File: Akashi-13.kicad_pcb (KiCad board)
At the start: 2 copper layers, 67.3 x 91.4 mm, 5 parts, among them J1 Conn_02x35_Odd_Even, J2 Conn_02x35_Odd_Even, J3 N7E50-Q516RB-50, J4 J0011D01BNL, U1 LAN9220-ABZJ

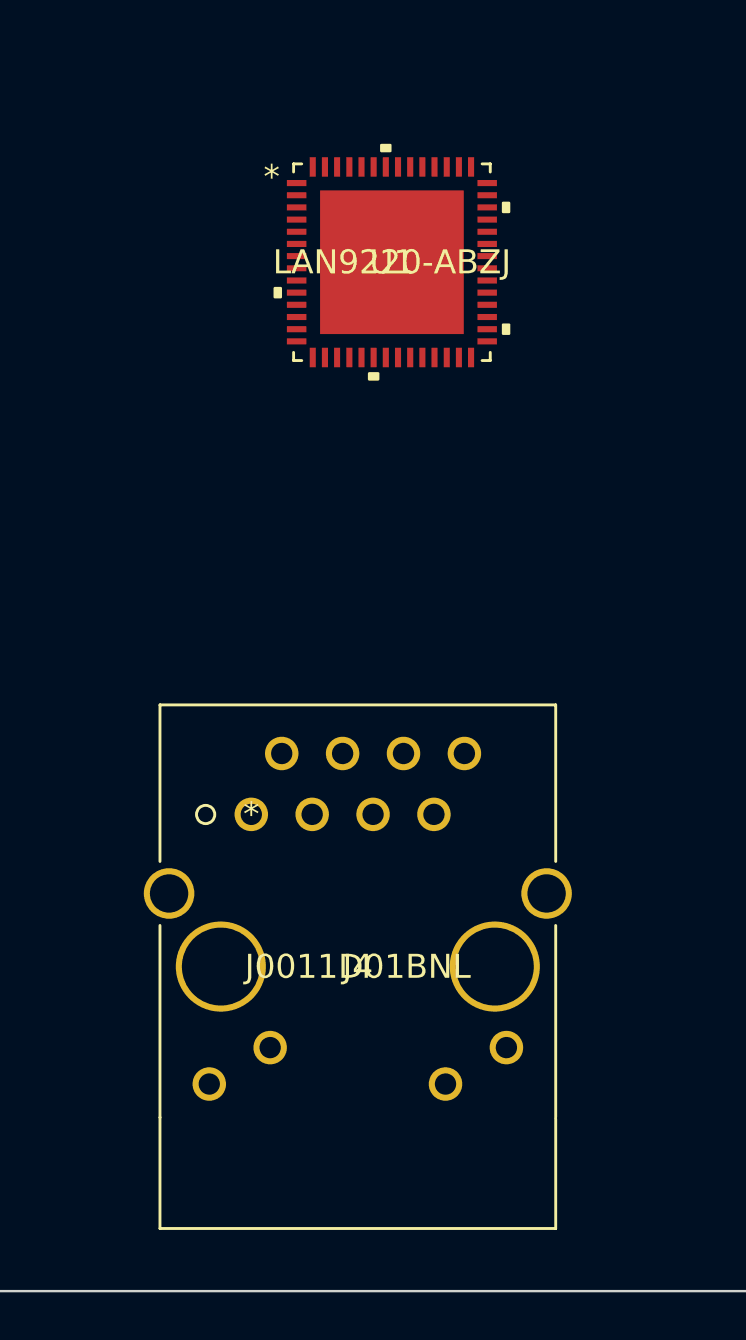
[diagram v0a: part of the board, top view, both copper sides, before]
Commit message: Drawing schematics.
Done round the RF-45 connectors.

Connecting the power of the LAN9220.
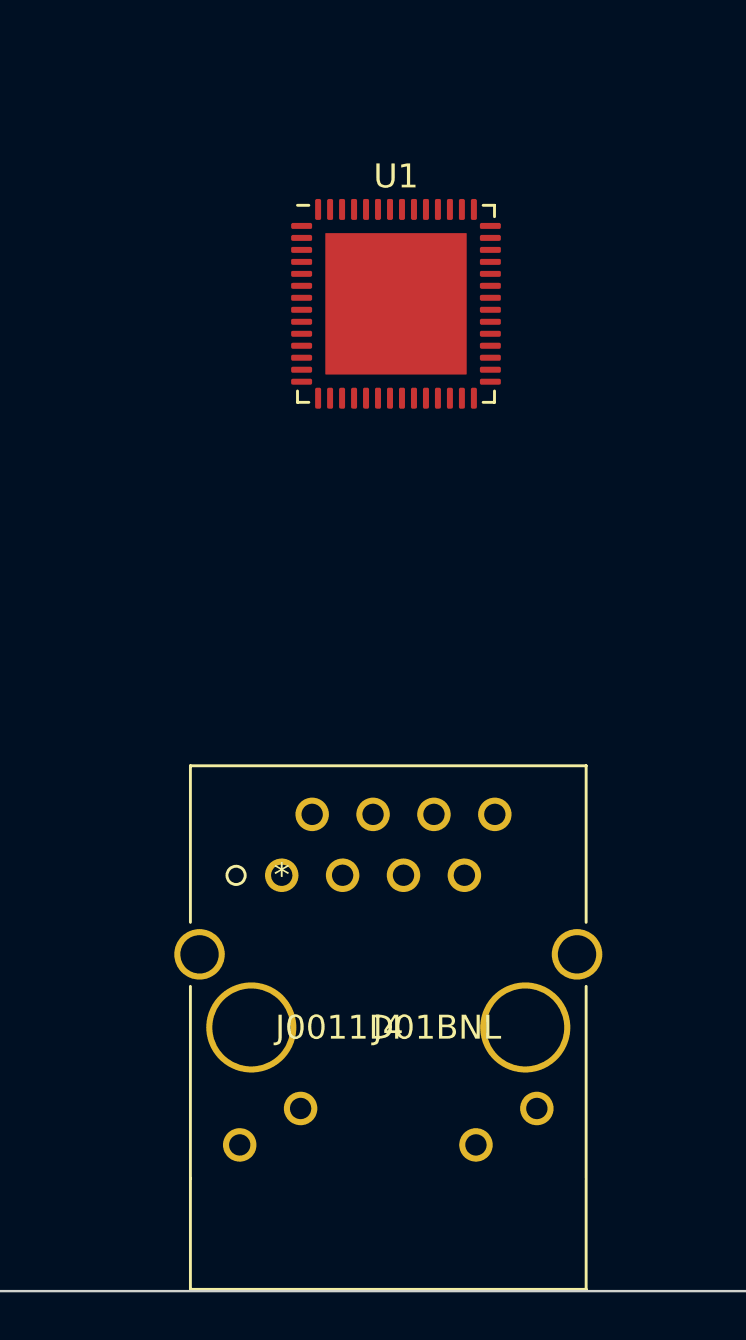
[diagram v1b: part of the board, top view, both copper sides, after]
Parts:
- U1: footprint MyFootprint:LAN9220-ABZJ -> Package_DFN_QFN:QFN-56-1EP_8x8mm_P0.5mm_EP5.9x5.9mm
- moved J4 2.84 mm to (127.5, 137.6)
- moved U1 1.74 mm to (132.2, 113.8)
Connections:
- J1 pad 14: unconnected-(J1-Pin_14-Pad14) -> /nRESET
- J1 pad 19: unconnected-(J1-Pin_19-Pad19) -> Net-(J1-Pin_19)
- J1 pad 20: unconnected-(J1-Pin_20-Pad20) -> Net-(J1-Pin_20)
- J1 pad 22: unconnected-(J1-Pin_22-Pad22) -> Net-(J1-Pin_20)
- J1 pad 39: unconnected-(J1-Pin_39-Pad39) -> /NOE
- J1 pad 41: unconnected-(J1-Pin_41-Pad41) -> /NWE
- J1 pad 49: unconnected-(J1-Pin_49-Pad49) -> Net-(J1-Pin_19)
- J1 pad 51: unconnected-(J1-Pin_51-Pad51) -> /A1
- J1 pad 52: unconnected-(J1-Pin_52-Pad52) -> /A2
- J1 pad 53: unconnected-(J1-Pin_53-Pad53) -> /A0
- J1 pad 55: unconnected-(J1-Pin_55-Pad55) -> /D3
- J1 pad 57: unconnected-(J1-Pin_57-Pad57) -> /D2
- J1 pad 60: unconnected-(J1-Pin_60-Pad60) -> Net-(J1-Pin_20)
- J1 pad 69: unconnected-(J1-Pin_69-Pad69) -> /D14
- J1 pad 8: unconnected-(J1-Pin_8-Pad8) -> Net-(J1-Pin_20)
- J2 pad 10: unconnected-(J2-Pin_10-Pad10) -> /D13
- J2 pad 18: unconnected-(J2-Pin_18-Pad18) -> /STLINK_RX
- J2 pad 19: unconnected-(J2-Pin_19-Pad19) -> /NE1
- J2 pad 2: unconnected-(J2-Pin_2-Pad2) -> /NE2
- J2 pad 20: unconnected-(J2-Pin_20-Pad20) -> Net-(J2-Pin_20)
- J2 pad 25: unconnected-(J2-Pin_25-Pad25) -> /STLINK_TX
- J2 pad 32: unconnected-(J2-Pin_32-Pad32) -> Net-(J2-Pin_20)
- J2 pad 36: unconnected-(J2-Pin_36-Pad36) -> /A5
- J2 pad 38: unconnected-(J2-Pin_38-Pad38) -> /A4
- J2 pad 39: unconnected-(J2-Pin_39-Pad39) -> Net-(J2-Pin_39)
- J2 pad 40: unconnected-(J2-Pin_40-Pad40) -> /D5
- J2 pad 44: unconnected-(J2-Pin_44-Pad44) -> /D4
- J2 pad 46: unconnected-(J2-Pin_46-Pad46) -> /D0
- J2 pad 47: unconnected-(J2-Pin_47-Pad47) -> /D7
- J2 pad 48: unconnected-(J2-Pin_48-Pad48) -> /D1
- J2 pad 49: unconnected-(J2-Pin_49-Pad49) -> /D9
- J2 pad 51: unconnected-(J2-Pin_51-Pad51) -> /D11
- J2 pad 52: unconnected-(J2-Pin_52-Pad52) -> /D6
- J2 pad 53: unconnected-(J2-Pin_53-Pad53) -> /D12
- J2 pad 54: unconnected-(J2-Pin_54-Pad54) -> Net-(J2-Pin_20)
- J2 pad 55: unconnected-(J2-Pin_55-Pad55) -> /D10
- J2 pad 56: unconnected-(J2-Pin_56-Pad56) -> /D8
- J2 pad 57: unconnected-(J2-Pin_57-Pad57) -> /A7
- J2 pad 58: unconnected-(J2-Pin_58-Pad58) -> /A3
- J2 pad 59: unconnected-(J2-Pin_59-Pad59) -> /A6
- J2 pad 63: unconnected-(J2-Pin_63-Pad63) -> Net-(J2-Pin_39)
- J2 pad 65: unconnected-(J2-Pin_65-Pad65) -> /D15
- J2 pad 9: unconnected-(J2-Pin_9-Pad9) -> Net-(J2-Pin_39)

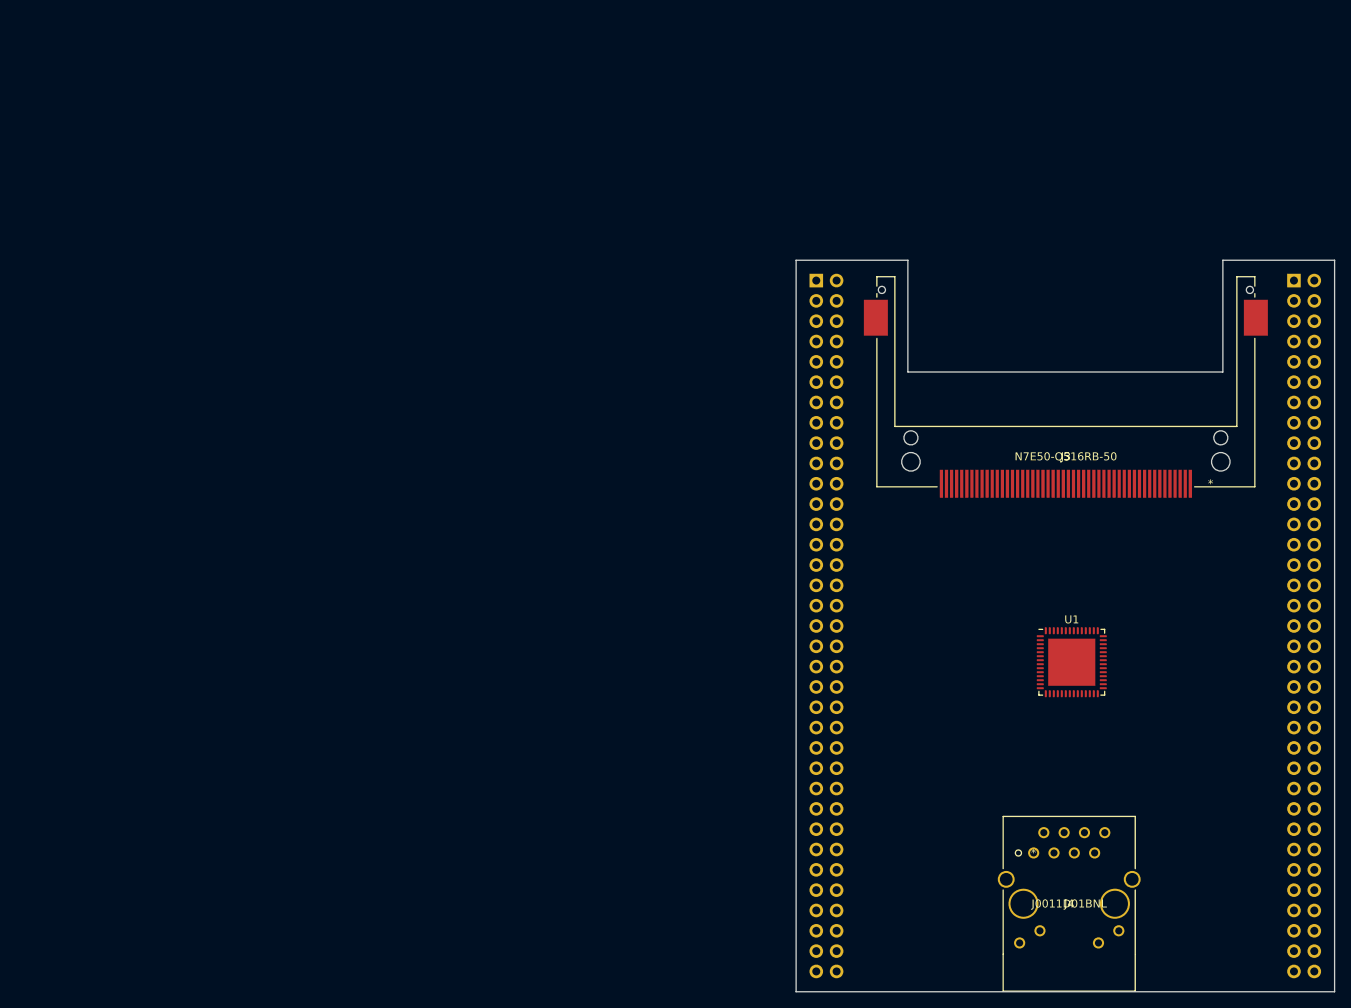
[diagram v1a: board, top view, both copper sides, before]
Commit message: ST Link VCOM changed. IRQ/WAKE UP changed.
ST LINK vcom are moved from USART3 to LPUART1
Now, we don't need extra wireling.
Alternatively, short bridged of the baord have to be modified.

IQR/WAKEUP pins are moved. Now. we can cut two extra pins of
morpho connectors to reduce the pin force.
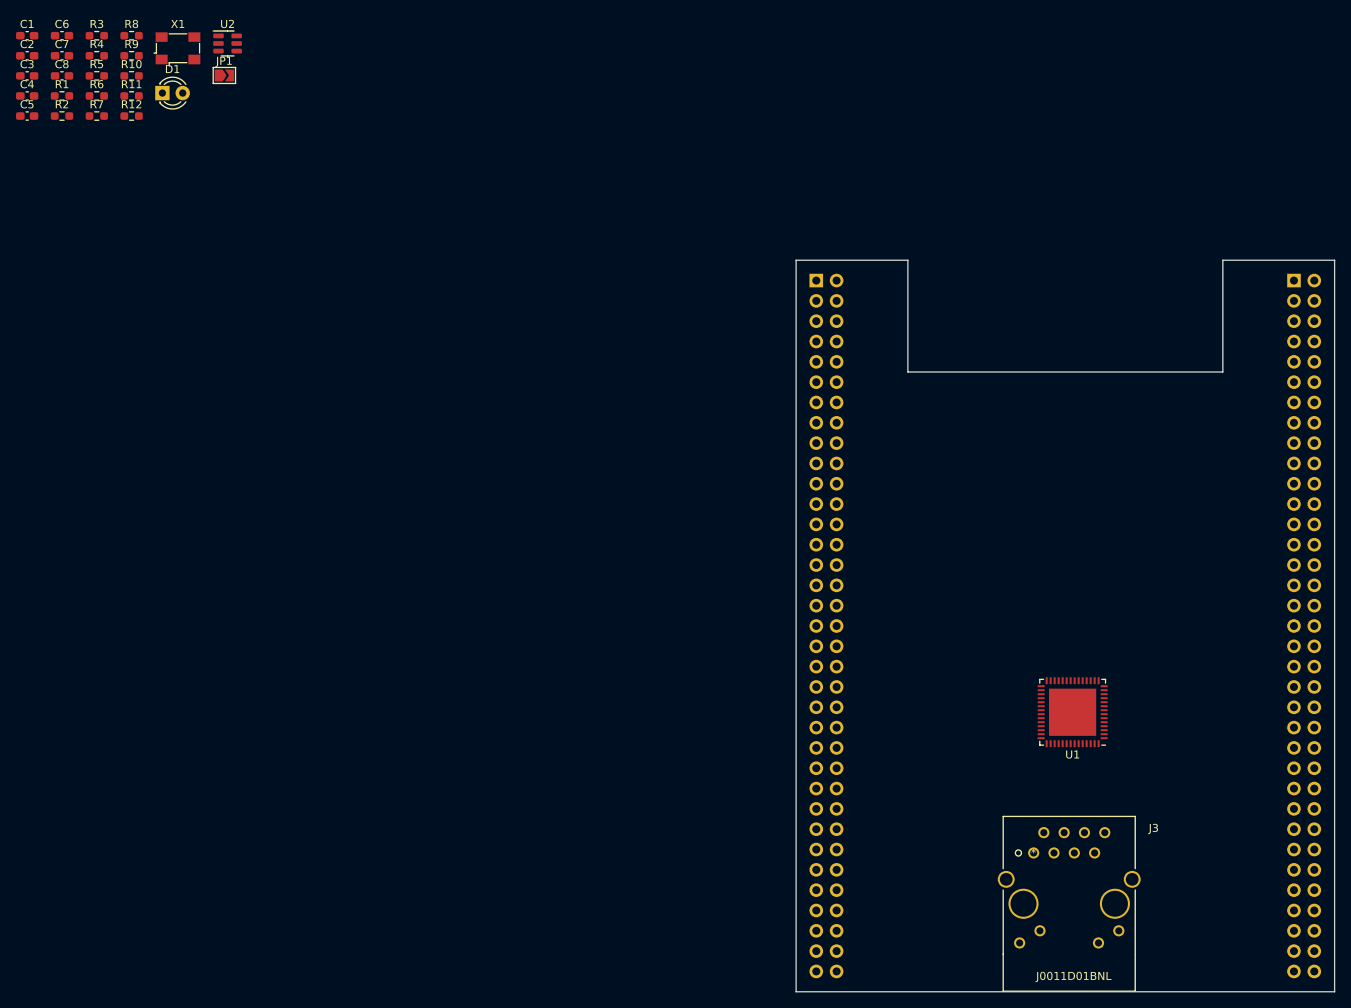
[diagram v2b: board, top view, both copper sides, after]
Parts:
- removed the J3 at (131.5, 88.0)
- added C1: C_Small, Capacitor_SMD:C_0603_1608Metric_Pad1.08x0.95mm_HandSolder, F.Cu at (1.68, 35.4)
- added C2: C_Small, Capacitor_SMD:C_0603_1608Metric_Pad1.08x0.95mm_HandSolder, F.Cu at (1.68, 37.9)
- added C3: C_Small, Capacitor_SMD:C_0603_1608Metric_Pad1.08x0.95mm_HandSolder, F.Cu at (1.68, 40.5)
- added C4: C_Small, Capacitor_SMD:C_0603_1608Metric_Pad1.08x0.95mm_HandSolder, F.Cu at (1.68, 43.0)
- added C5: C_Small, Capacitor_SMD:C_0603_1608Metric_Pad1.08x0.95mm_HandSolder, F.Cu at (1.68, 45.5)
- added C6: C_Small, Capacitor_SMD:C_0603_1608Metric_Pad1.08x0.95mm_HandSolder, F.Cu at (6.03, 35.4)
- added C7: C_Small, Capacitor_SMD:C_0603_1608Metric_Pad1.08x0.95mm_HandSolder, F.Cu at (6.03, 37.9)
- added C8: C_Small, Capacitor_SMD:C_0603_1608Metric_Pad1.08x0.95mm_HandSolder, F.Cu at (6.03, 40.5)
- added D1: LED, LED_THT:LED_D3.0mm, F.Cu at (18.6, 42.6)
- added JP1: SolderJumper_2_Open, Jumper:SolderJumper-2_P1.3mm_Open_TrianglePad1.0x1.5mm, F.Cu at (26.3, 40.4)
- added R1: R, Resistor_SMD:R_0603_1608Metric_Pad0.98x0.95mm_HandSolder, F.Cu at (6.03, 43.0)
- added R10: R, Resistor_SMD:R_0603_1608Metric_Pad0.98x0.95mm_HandSolder, F.Cu at (14.7, 40.5)
- added R11: R, Resistor_SMD:R_0603_1608Metric_Pad0.98x0.95mm_HandSolder, F.Cu at (14.7, 43.0)
- added R12: R, Resistor_SMD:R_0603_1608Metric_Pad0.98x0.95mm_HandSolder, F.Cu at (14.7, 45.5)
- added R2: R, Resistor_SMD:R_0603_1608Metric_Pad0.98x0.95mm_HandSolder, F.Cu at (6.03, 45.5)
- added R3: R, Resistor_SMD:R_0603_1608Metric_Pad0.98x0.95mm_HandSolder, F.Cu at (10.4, 35.4)
- added R4: R, Resistor_SMD:R_0603_1608Metric_Pad0.98x0.95mm_HandSolder, F.Cu at (10.4, 37.9)
- added R5: R, Resistor_SMD:R_0603_1608Metric_Pad0.98x0.95mm_HandSolder, F.Cu at (10.4, 40.5)
- added R6: R, Resistor_SMD:R_0603_1608Metric_Pad0.98x0.95mm_HandSolder, F.Cu at (10.4, 43.0)
- added R7: R, Resistor_SMD:R_0603_1608Metric_Pad0.98x0.95mm_HandSolder, F.Cu at (10.4, 45.5)
- added R8: R, Resistor_SMD:R_0603_1608Metric_Pad0.98x0.95mm_HandSolder, F.Cu at (14.7, 35.4)
- added R9: R, Resistor_SMD:R_0603_1608Metric_Pad0.98x0.95mm_HandSolder, F.Cu at (14.7, 37.9)
- added U2: 93AA46AT-IOT, Package_TO_SOT_SMD:SOT-23-6, F.Cu at (26.7, 36.4)
- added X1: DFA-S15, Oscillator:Oscillator_SMD_Fordahl_DFAS15-4Pin_5.0x3.2mm, F.Cu at (20.5, 37.0)
- moved U1 6.25 mm to (132.4, 120.0), turned to 180 degrees
- renumbered J4 to J3
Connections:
- J1 pad 16: unconnected-(J1-Pin_16-Pad16) -> +3.3V
- J1 pad 19: Net-(J1-Pin_19) -> GND
- J1 pad 20: Net-(J1-Pin_20) -> GND
- J1 pad 22: Net-(J1-Pin_20) -> GND
- J1 pad 28: unconnected-(J1-Pin_28-Pad28) -> /WAKEUP
- J1 pad 32: unconnected-(J1-Pin_32-Pad32) -> /IRQ
- J1 pad 39: /NOE -> /nOE
- J1 pad 41: /NWE -> /nWE
- J1 pad 49: Net-(J1-Pin_19) -> GND
- J1 pad 60: Net-(J1-Pin_20) -> GND
- J1 pad 8: Net-(J1-Pin_20) -> GND
- J2 pad 18: /STLINK_RX -> unconnected-(J2-Pin_18-Pad18)
- J2 pad 19: /NE1 -> /nE1
- J2 pad 2: /NE2 -> unconnected-(J2-Pin_2-Pad2)
- J2 pad 20: Net-(J2-Pin_20) -> GND
- J2 pad 25: /STLINK_TX -> unconnected-(J2-Pin_25-Pad25)
- J2 pad 32: Net-(J2-Pin_20) -> GND
- J2 pad 39: Net-(J2-Pin_39) -> GND
- J2 pad 54: Net-(J2-Pin_20) -> GND
- J2 pad 63: Net-(J2-Pin_39) -> GND
- J2 pad 9: Net-(J2-Pin_39) -> GND
- J3 pad 1: unconnected-(J4-Pad1) -> /TD+
- J3 pad 10: unconnected-(J4-Pad10) -> /nLNK_ACT
- J3 pad 11: unconnected-(J4-Pad11) -> /nSPD100
- J3 pad 12: unconnected-(J4-Pad12) -> Net-(J3-Pad12)
- J3 pad 2: unconnected-(J4-Pad2) -> /TD-
- J3 pad 3: unconnected-(J4-Pad3) -> /RD+
- J3 pad 4: unconnected-(J4-Pad4) -> GND
- J3 pad 5: unconnected-(J4-Pad5) -> GND
- J3 pad 6: unconnected-(J4-Pad6) -> /RD-
- J3 pad 7: unconnected-(J4-Pad7) -> GND
- J3 pad 8: unconnected-(J4-Pad8) -> GND
- J3 pad 9: unconnected-(J4-Pad9) -> Net-(J3-Pad9)
- U1 pad 1: unconnected-(U1-VDD33REG-Pad1) -> +3.3V
- U1 pad 10: unconnected-(U1-A3-Pad10) -> /A3
- U1 pad 11: unconnected-(U1-A2-Pad11) -> /A2
- U1 pad 12: unconnected-(U1-A1-Pad12) -> /A1
- U1 pad 13: unconnected-(U1-FIFO_SEL-Pad13) -> GND
- U1 pad 14: unconnected-(U1-TEST-Pad14) -> GND
- U1 pad 15: unconnected-(U1-NRD-Pad15) -> /nOE
- U1 pad 16: unconnected-(U1-NWR-Pad16) -> /nWE
- U1 pad 17: unconnected-(U1-NCS-Pad17) -> /nE1
- U1 pad 18: unconnected-(U1-VDDVARIO-Pad18) -> +3.3V
- U1 pad 19: unconnected-(U1-D15-Pad19) -> /D15
- U1 pad 2: unconnected-(U1-VDD18CORE-Pad2) -> +1V8
- U1 pad 20: unconnected-(U1-D14-Pad20) -> /D14
- U1 pad 21: unconnected-(U1-D13-Pad21) -> /D13
- U1 pad 22: unconnected-(U1-D12-Pad22) -> /D12
- U1 pad 23: unconnected-(U1-D11-Pad23) -> /D11
- U1 pad 24: unconnected-(U1-VDDVARIO-Pad24) -> +3.3V
- U1 pad 25: unconnected-(U1-D10-Pad25) -> /D10
- U1 pad 26: unconnected-(U1-D9-Pad26) -> /D9
- U1 pad 27: unconnected-(U1-D8-Pad27) -> /D8
- U1 pad 28: unconnected-(U1-D7-Pad28) -> /D7
- U1 pad 29: unconnected-(U1-D6-Pad29) -> /D6
- U1 pad 3: unconnected-(U1-GPIO0/NLED1-Pad3) -> /nSPD100
- U1 pad 30: unconnected-(U1-VDDVARIO-Pad30) -> +3.3V
- U1 pad 31: unconnected-(U1-D5-Pad31) -> /D5
- U1 pad 32: unconnected-(U1-D4-Pad32) -> /D4
- U1 pad 33: unconnected-(U1-D3-Pad33) -> /D3
- U1 pad 34: unconnected-(U1-D2-Pad34) -> /D2
- U1 pad 35: unconnected-(U1-D1-Pad35) -> /D1
- U1 pad 36: unconnected-(U1-D0-Pad36) -> /D0
- U1 pad 37: unconnected-(U1-VDD18CORE-Pad37) -> +1V8
- U1 pad 38: unconnected-(U1-EEDIO/GPO3-Pad38) -> /EEP_DIO
- U1 pad 39: unconnected-(U1-EECS-Pad39) -> /EEP_CS
- U1 pad 4: unconnected-(U1-GPIO1/NLED2-Pad4) -> /nLNK_ACT
- U1 pad 40: unconnected-(U1-EECLK/GPO4-Pad40) -> /EEP_CLK
- U1 pad 41: unconnected-(U1-PME-Pad41) -> /WAKEUP
- U1 pad 42: unconnected-(U1-NRESET-Pad42) -> /nRESET
- U1 pad 43: unconnected-(U1-IRQ-Pad43) -> /IRQ
- U1 pad 44: unconnected-(U1-TPO--Pad44) -> /TD-
- U1 pad 45: unconnected-(U1-TPO+-Pad45) -> /TD+
- U1 pad 46: unconnected-(U1-VDD33A-Pad46) -> +3.3V
- U1 pad 47: unconnected-(U1-TPI--Pad47) -> /RD-
- U1 pad 48: unconnected-(U1-TPI+-Pad48) -> /RD+
- U1 pad 49: unconnected-(U1-VDD33A-Pad49) -> +3.3V
- U1 pad 5: unconnected-(U1-GPIO2/LED3-Pad5) -> /nFPDLX
- U1 pad 50: unconnected-(U1-EXRES-Pad50) -> Net-(U1-EXRES)
- U1 pad 51: unconnected-(U1-VDD33A-Pad51) -> +3.3V
- U1 pad 52: unconnected-(U1-AMDIX_EN-Pad52) -> /AMDIX_EN
- U1 pad 53: unconnected-(U1-VDD18A-Pad53) -> +1V8
- U1 pad 55: unconnected-(U1-XTAL1/CLKIN-Pad55) -> Net-(U1-XTAL1/CLKIN)
- U1 pad 56: unconnected-(U1-VDDVARIO-Pad56) -> +3.3V
- U1 pad 57: unconnected-(U1-EPAD-Pad57) -> GND
- U1 pad 6: unconnected-(U1-A7-Pad6) -> /A7
- U1 pad 7: unconnected-(U1-A6-Pad7) -> /A6
- U1 pad 8: unconnected-(U1-A5-Pad8) -> /A5
- U1 pad 9: unconnected-(U1-A4-Pad9) -> /A4
